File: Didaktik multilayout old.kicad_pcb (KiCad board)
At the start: 2 copper layers, 212.7 x 79.4 mm, 121 parts, among them J1 Conn_01x04_MountingPin, J2 AVR-ISP-6, SW1 SW_Push_45deg, SW10 SW_Push_45deg, SW11 SW_Push_45deg, SW12 SW_Push_45deg, SW13 SW_Push_45deg, SW14 SW_Push_45deg, SW15 SW_Push_45deg, SW16 SW_Push_45deg, SW17 SW_Push_45deg, SW18 SW_Push_45deg, SW19 SW_Push_45deg, SW2 SW_Push_45deg, SW20 SW_Push_45deg, SW21 SW_Push_45deg, SW22 SW_Push_45deg, SW23 SW_Push_45deg, SW24 SW_Push_45deg, SW25 SW_Push_45deg, SW26 SW_Push_45deg, SW27 SW_Push_45deg, SW28 SW_Push_45deg, SW29 SW_Push_45deg, SW3 SW_Push_45deg, SW30 SW_Push_45deg, SW31 SW_Push_45deg, SW31a1 SW_Push_45deg, SW32 SW_Push_45deg, SW32a1 SW_Push_45deg, SW33 SW_Push_45deg, SW33a1 SW_Push_45deg, SW34 SW_Push_45deg, SW34a1 SW_Push_45deg, SW34b1 SW_Push_45deg, SW35 SW_Push_45deg, SW35a1 SW_Push_45deg, SW35b1 SW_Push_45deg, SW35c1 SW_Push_45deg, SW36 SW_Push_45deg, SW36a1 SW_Push_45deg, SW36b1 SW_Push_45deg, SW36c1 SW_Push_45deg, SW37 SW_Push_45deg, SW37a1 SW_Push_45deg, SW37b1 SW_Push_45deg, SW38 SW_Push_45deg, SW38a1 SW_Push_45deg, SW39 SW_Push_45deg, SW39a1 SW_Push_45deg, SW4 SW_Push_45deg, SW40 SW_Push_45deg, SW40a1 SW_Push_45deg, SW5 SW_Push_45deg, SW6 SW_Push_45deg, SW7 SW_Push_45deg, SW8 SW_Push_45deg, SW9 SW_Push_45deg, U1 ATmega32U4-M, Y1 Crystal_GND24_Small

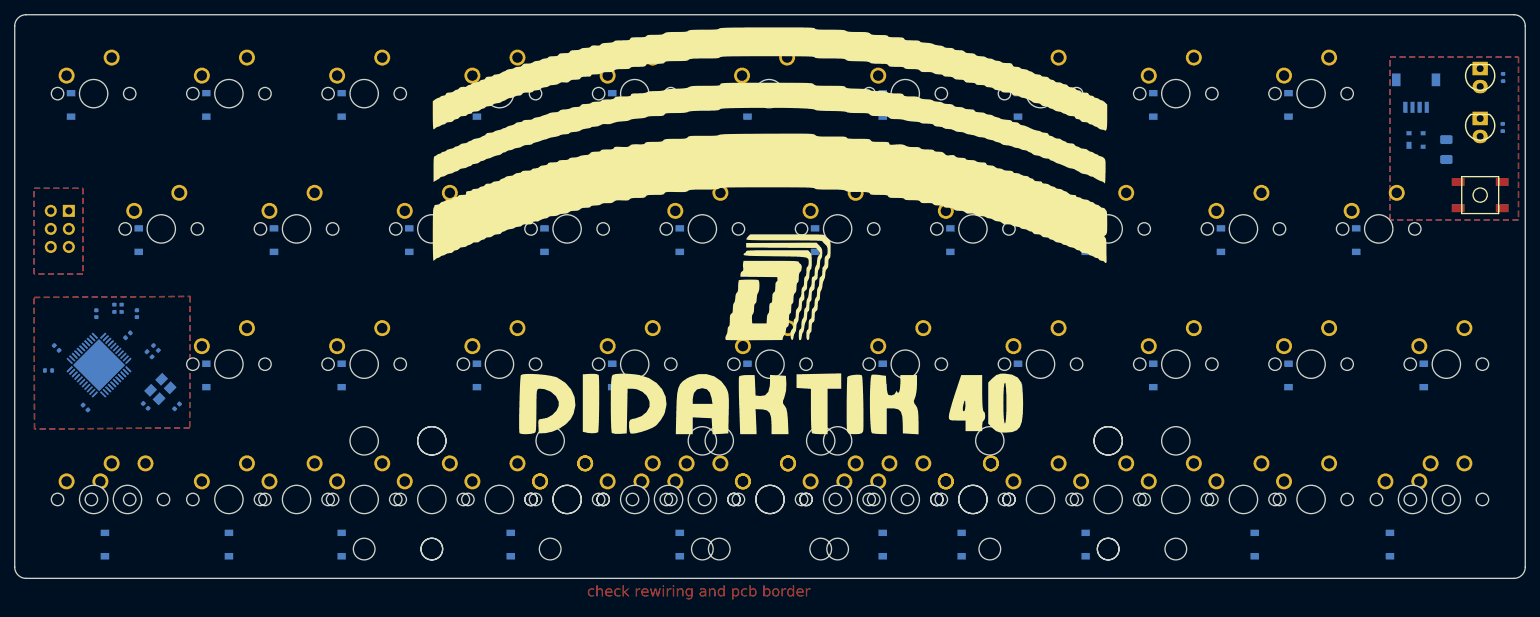
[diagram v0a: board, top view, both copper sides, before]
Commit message: pcb copy, footprint revision, rerouting needed
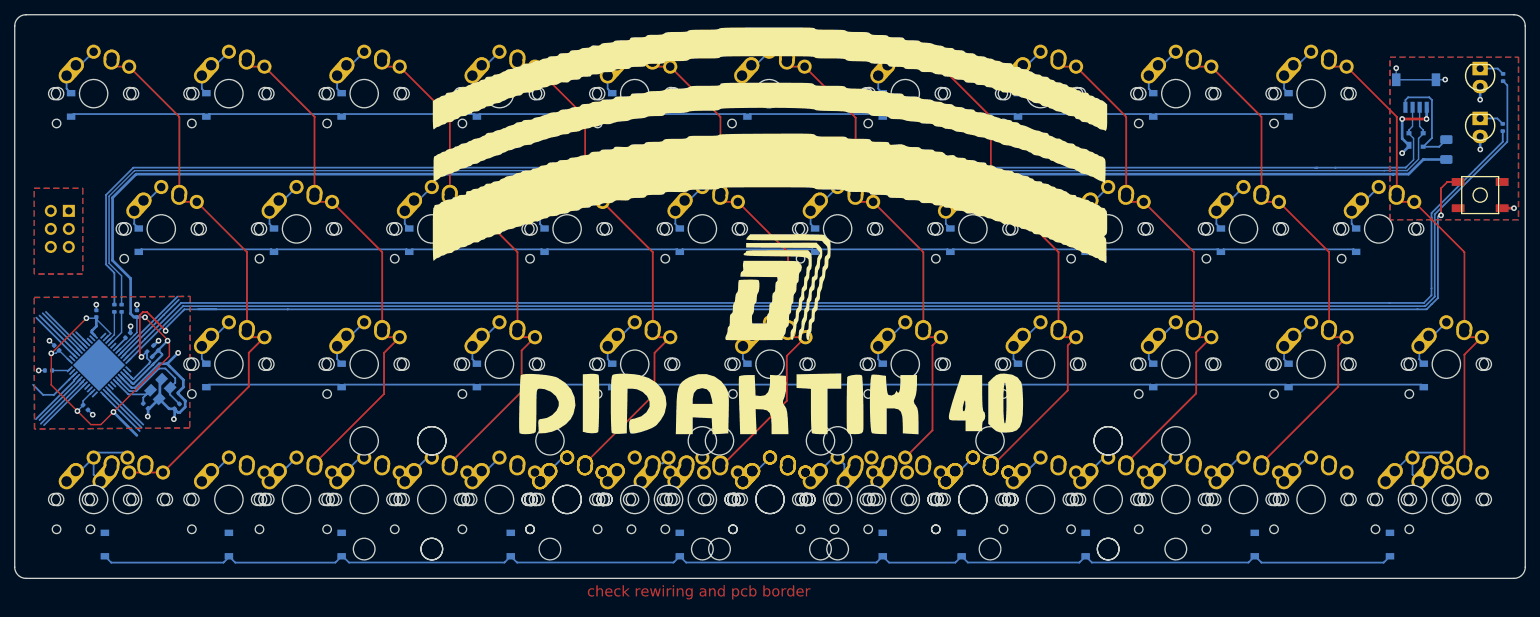
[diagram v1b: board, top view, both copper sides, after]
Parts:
- SW1, SW10, SW11, SW12, SW13, SW14, SW15, SW16, SW17, SW18, SW19, SW2, SW20, SW21, SW22, SW23, SW24, SW25, SW26, SW27, SW28, SW29, SW3, SW30, SW31a1, SW32, SW32a1, SW33, SW33a1, SW34, SW34a1, SW35, SW36, SW37, SW37a1, SW38, SW38a1, SW39, SW39a1, SW4, SW40a1, SW5, SW6, SW7, SW8, SW9: footprint MX_Only:MXOnly-1U-NoLED -> Keebio-Parts:MX-Alps-Choc-1U-NoLED
- SW31, SW35a1, SW36a1, SW40: footprint MX_Only:MXOnly-1.5U-NoLED -> Keebio-Parts:MX-Alps-Choc-1.5U-NoLED
- SW34b1, SW37b1: footprint MX_Only:MXOnly-3U-ReversedStabilizers-NoLED -> Keebio-Parts:MX-Alps-Choc-3U-NoLED-StabFlip
- SW35b1, SW36b1: footprint MX_Only:MXOnly-2U-ReversedStabilizers-NoLED -> Keebio-Parts:MX-Alps-Choc-2U-NoLED-StabFlip
- SW35c1: footprint MX_Only:MXOnly-6U-Centered-ReversedStabilizers-NoLED -> Keebio-Parts:MX-Alps-Choc-6U-NoLED-StabFlip
- SW36c1: footprint MX_Only:MXOnly-7U-ReversedStabilizers-NoLED -> Keebio-Parts:MX-Alps-Choc-7U-NoLED-StabFlip
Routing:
- net +5V: track 0.00 -> 289.5 mm, vias 0 -> 6
- net LED capslock: track 0.00 -> 222.5 mm
- net RESET: track 0.00 -> 221.2 mm, vias 0 -> 3
- net LED Power: track 0.00 -> 215.2 mm
- net D+: track 0.00 -> 210.4 mm
- net D-: track 0.00 -> 210.3 mm
- net ROW3: track 0.00 -> 199.0 mm
- net ROW2: track 0.00 -> 185.3 mm
- net ROW1: track 0.00 -> 176.5 mm
- net ROW0: track 0.00 -> 176.4 mm
- net COL0: track 0.00 -> 89.1 mm
- net COL6: track 0.00 -> 83.3 mm
- net COL8: track 0.00 -> 82.7 mm
- net COL4: track 0.00 -> 82.5 mm
- net COL7: track 0.00 -> 82.4 mm
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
